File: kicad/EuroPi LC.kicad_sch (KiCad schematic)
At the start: 2 parts, among them U4 MOUDLE-SEEEDUINO-XIAO

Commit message: make 4hp
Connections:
- net VSYS renamed +5V
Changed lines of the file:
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@@
   (junction (at 36.83 55.88) (diameter 0) (color 0 0 0 0)
+  )
+  (wire (pts (xy 114.3 40.64) (xy 114.3 33.02))
+    (stroke (width 0) (type default))
   )
   (wire (pts (xy 121.92 38.1) (xy 121.92 45.72))
@@
   )
   (wire (pts (xy 36.83 55.88) (xy 36.83 63.5))
+    (stroke (width 0) (type default))
+  )
+  (wire (pts (xy 107.95 40.64) (xy 114.3 40.64))
     (stroke (width 0) (type default))
   )
@@
     )
   )
-  (global_label "VSYS" (shape input) (at 107.95 40.64 0) (fields_autoplaced)
-    (effects (font (size 1.27 1.27)) (justify left))
-    (property "Intersheetrefs" "${INTERSHEET_REFS}" (at 115.452 40.64 0)
-      (effects (font (size 1.27 1.27)) (justify left) hide)
-    )
-  )
   (global_label "BUTTON_2" (shape input) (at 67.31 53.34 180) (fields_autoplaced)
     (effects (font (size 1.27 1.27)) (justify right))
@@
         )
       )
+    )
+  )
+  (symbol (lib_id "power:+5V") (at 114.3 33.02 0) (unit 1)
+    (in_bom yes) (on_board yes) (dnp no) (fields_autoplaced)
+    (property "Reference" "#PWR038" (at 114.3 36.83 0)
+      (effects (font (size 1.27 1.27)) hide)
+    )
+    (property "Value" "+5V" (at 114.3 29.21 0)
+      (effects (font (size 1.27 1.27)))
+    )
+    (property "Footprint" "" (at 114.3 33.02 0)
+      (effects (font (size 1.27 1.27)) hide)
+    )
+    (property "Datasheet" "" (at 114.3 33.02 0)
+      (effects (font (size 1.27 1.27)) hide)
+    )
+    (pin "1")
+    (instances
+      (project "EuroPi LC"
+        (path "/1702e620-a749-4340-9e49-cfdb2636cab7/2c8ccfa5-26eb-4a4b-90f9-a487a325ddf4"
+          (reference "#PWR038") (unit 1)
+        )
+        (path "/1702e620-a749-4340-9e49-cfdb2636cab7"
+          (reference "#PWR039") (unit 1)
+        )
+      )

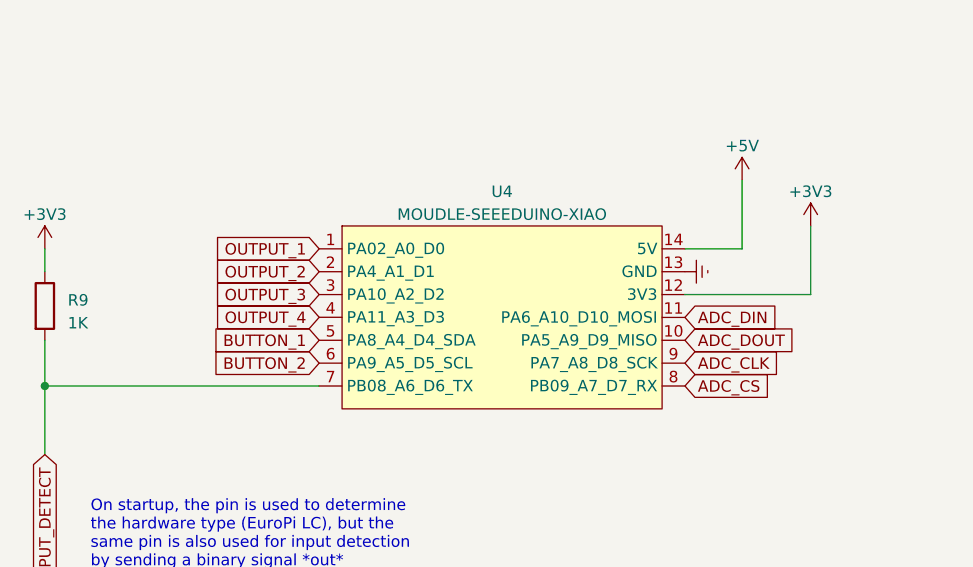
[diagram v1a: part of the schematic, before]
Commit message: input changes
use single channel ADCs for analog inputs and knob 1 which use i2c instead of SPI to free up one pin for input 1 to be used as a digital input as well
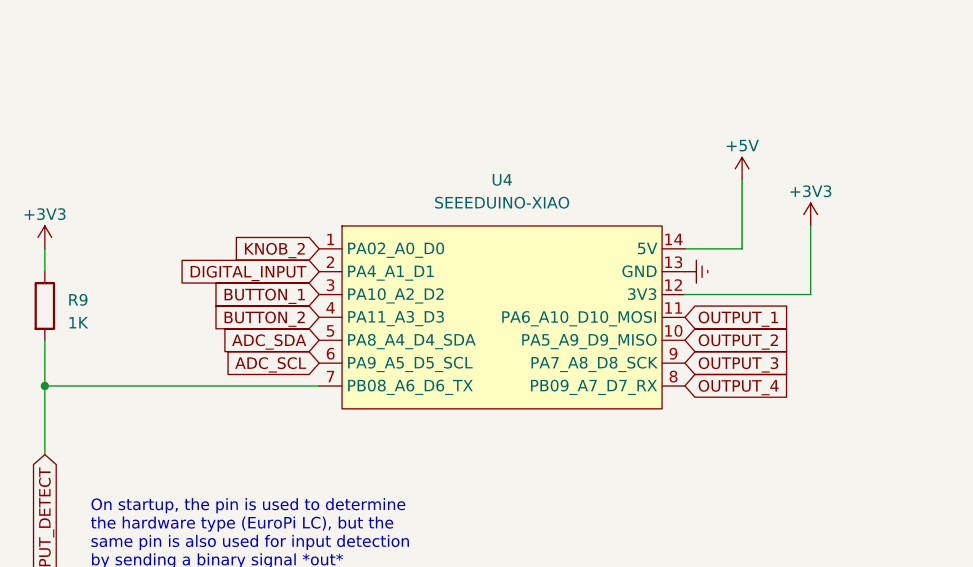
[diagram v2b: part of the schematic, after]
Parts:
- U4: value MOUDLE-SEEEDUINO-XIAO -> SEEEDUINO-XIAO
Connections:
- net ADC_CLK is gone; now on net OUTPUT_3: U4.9 (PA7_A8_D8_SCK)
- net ADC_DIN is gone; now on net OUTPUT_1: U4.11 (PA6_A10_D10_MOSI)
- net ADC_DOUT is gone; now on net OUTPUT_2: U4.10 (PA5_A9_D9_MISO)
- net BUTTON_1: now also U4.3 (PA10_A2_D2); no longer U4.5 (PA8_A4_D4_SDA)
- net BUTTON_2: no longer U4.6 (PA9_A5_D5_SCL)
- net OUTPUT_1: no longer U4.1 (PA02_A0_D0)
- net OUTPUT_2: no longer U4.2 (PA4_A1_D1)
- net OUTPUT_3: no longer U4.3 (PA10_A2_D2)
- net OUTPUT_4: no longer U4.4 (PA11_A3_D3)
- net ADC_CS: no longer names the net of U4.8 (PB09_A7_D7_RX)
- new net ADC_SCL: U4.6 (PA9_A5_D5_SCL)
- new net ADC_SDA: U4.5 (PA8_A4_D4_SDA)
- new net DIGITAL_INPUT: U4.2 (PA4_A1_D1)
- new net KNOB_2: U4.1 (PA02_A0_D0)
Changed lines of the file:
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@@
     (effects (font (size 1.27 1.27)) (justify left bottom))
   )
-  (global_label "ADC_CS" (shape input) (at 107.95 55.88 0) (fields_autoplaced)
-    (effects (font (size 1.27 1.27)) (justify left))
-    (property "Intersheetrefs" "${INTERSHEET_REFS}" (at 117.9315 55.88 0)
-      (effects (font (size 1.27 1.27)) (justify left) hide)
-    )
-  )
-  (global_label "ADC_CLK" (shape input) (at 107.95 53.34 0) (fields_autoplaced)
-    (effects (font (size 1.27 1.27)) (justify left))
-    (property "Intersheetrefs" "${INTERSHEET_REFS}" (at 119.0201 53.34 0)
-      (effects (font (size 1.27 1.27)) (justify left) hide)
-    )
-  )
-  (global_label "OUTPUT_3" (shape input) (at 67.31 45.72 180) (fields_autoplaced)
+  (global_label "OUTPUT_3" (shape input) (at 107.95 53.34 0) (fields_autoplaced)
+    (effects (font (size 1.27 1.27)) (justify left))
+    (property "Intersheetrefs" "${INTERSHEET_REFS}" (at 120.2296 53.34 0)
+      (effects (font (size 1.27 1.27)) (justify left) hide)
+    )
+  )
+  (global_label "OUTPUT_1" (shape input) (at 107.95 48.26 0) (fields_autoplaced)
+    (effects (font (size 1.27 1.27)) (justify left))
+    (property "Intersheetrefs" "${INTERSHEET_REFS}" (at 120.2296 48.26 0)
+      (effects (font (size 1.27 1.27)) (justify left) hide)
+    )
+  )
+  (global_label "INPUT_DETECT" (shape input) (at 36.83 63.5 270) (fields_autoplaced)
+    (effects (font (size 1.27 1.27)) (justify right))
+    (property "Intersheetrefs" "${INTERSHEET_REFS}" (at 36.83 79.65 90)
+      (effects (font (size 1.27 1.27)) (justify right) hide)
+    )
+  )
+  (global_label "OUTPUT_2" (shape input) (at 107.95 50.8 0) (fields_autoplaced)
+    (effects (font (size 1.27 1.27)) (justify left))
+    (property "Intersheetrefs" "${INTERSHEET_REFS}" (at 120.2296 50.8 0)
+      (effects (font (size 1.27 1.27)) (justify left) hide)
+    )
+  )
+  (global_label "KNOB_2" (shape input) (at 67.31 40.64 180) (fields_autoplaced)
+    (effects (font (size 1.27 1.27)) (justify right))
+    (property "Intersheetrefs" "${INTERSHEET_REFS}" (at 57.0261 40.64 0)
+      (effects (font (size 1.27 1.27)) (justify right) hide)
+    )
+  )
+  (global_label "ADC_SCL" (shape input) (at 67.31 53.34 180) (fields_autoplaced)
+    (effects (font (size 1.27 1.27)) (justify right))
+    (property "Intersheetrefs" "${INTERSHEET_REFS}" (at 56.3004 53.34 0)
+      (effects (font (size 1.27 1.27)) (justify right) hide)
+    )
+  )
+  (global_label "BUTTON_1" (shape input) (at 67.31 45.72 180) (fields_autoplaced)
     (effects (font (size 1.27 1.27)) (justify right))
     (property "Intersheetrefs" "${INTERSHEET_REFS}" (at 55.0304 45.72 0)
@@
     )
   )
-  (global_label "OUTPUT_1" (shape input) (at 67.31 40.64 180) (fields_autoplaced)
-    (effects (font (size 1.27 1.27)) (justify right))
-    (property "Intersheetrefs" "${INTERSHEET_REFS}" (at 55.0304 40.64 0)
-      (effects (font (size 1.27 1.27)) (justify right) hide)
-    )
-  )
-  (global_label "INPUT_DETECT" (shape input) (at 36.83 63.5 270) (fields_autoplaced)
-    (effects (font (size 1.27 1.27)) (justify right))
-    (property "Intersheetrefs" "${INTERSHEET_REFS}" (at 36.83 79.65 90)
-      (effects (font (size 1.27 1.27)) (justify right) hide)
-    )
-  )
-  (global_label "OUTPUT_2" (shape input) (at 67.31 43.18 180) (fields_autoplaced)
-    (effects (font (size 1.27 1.27)) (justify right))
-    (property "Intersheetrefs" "${INTERSHEET_REFS}" (at 55.0304 43.18 0)
-      (effects (font (size 1.27 1.27)) (justify right) hide)
-    )
-  )
-  (global_label "BUTTON_1" (shape input) (at 67.31 50.8 180) (fields_autoplaced)
-    (effects (font (size 1.27 1.27)) (justify right))
-    (property "Intersheetrefs" "${INTERSHEET_REFS}" (at 55.0304 50.8 0)
-      (effects (font (size 1.27 1.27)) (justify right) hide)
-    )
-  )
-  (global_label "ADC_DOUT" (shape input) (at 107.95 50.8 0) (fields_autoplaced)
-    (effects (font (size 1.27 1.27)) (justify left))
-    (property "Intersheetrefs" "${INTERSHEET_REFS}" (at 120.3506 50.8 0)
-      (effects (font (size 1.27 1.27)) (justify left) hide)
-    )
-  )
-  (global_label "ADC_DIN" (shape input) (at 107.95 48.26 0) (fields_autoplaced)
-    (effects (font (size 1.27 1.27)) (justify left))
-    (property "Intersheetrefs" "${INTERSHEET_REFS}" (at 118.6573 48.26 0)
-      (effects (font (size 1.27 1.27)) (justify left) hide)
-    )
-  )
-  (global_label "BUTTON_2" (shape input) (at 67.31 53.34 180) (fields_autoplaced)
-    (effects (font (size 1.27 1.27)) (justify right))
-    (property "Intersheetrefs" "${INTERSHEET_REFS}" (at 55.0304 53.34 0)
-      (effects (font (size 1.27 1.27)) (justify right) hide)
-    )
-  )
-  (global_label "OUTPUT_4" (shape input) (at 67.3132 48.2449 180) (fields_autoplaced)
-    (effects (font (size 1.27 1.27)) (justify right))
-    (property "Intersheetrefs" "${INTERSHEET_REFS}" (at 55.0336 48.2449 0)
-      (effects (font (size 1.27 1.27)) (justify right) hide)
+  (global_label "DIGITAL_INPUT" (shape input) (at 67.31 43.18 180) (fields_autoplaced)
+    (effects (font (size 1.27 1.27)) (justify right))
+    (property "Intersheetrefs" "${INTERSHEET_REFS}" (at 51.0993 43.18 0)
+      (effects (font (size 1.27 1.27)) (justify right) hide)
+    )
+  )
+  (global_label "ADC_SDA" (shape input) (at 67.31 50.8 180) (fields_autoplaced)
+    (effects (font (size 1.27 1.27)) (justify right))
+    (property "Intersheetrefs" "${INTERSHEET_REFS}" (at 56.2399 50.8 0)
+      (effects (font (size 1.27 1.27)) (justify right) hide)
+    )
+  )
+  (global_label "BUTTON_2" (shape input) (at 67.31 48.26 180) (fields_autoplaced)
+    (effects (font (size 1.27 1.27)) (justify right))
+    (property "Intersheetrefs" "${INTERSHEET_REFS}" (at 55.0304 48.26 0)
+      (effects (font (size 1.27 1.27)) (justify right) hide)
+    )
+  )
+  (global_label "OUTPUT_4" (shape input) (at 107.9468 55.8649 0) (fields_autoplaced)
+    (effects (font (size 1.27 1.27)) (justify left))
+    (property "Intersheetrefs" "${INTERSHEET_REFS}" (at 120.2264 55.8649 0)
+      (effects (font (size 1.27 1.27)) (justify left) hide)
     )
   )
@@
   (symbol (lib_id "MOUDLE-SEEEDUINO-XIAO:MOUDLE-SEEEDUINO-XIAO") (at 86.36 48.26 0) (unit 1)
     (in_bom yes) (on_board yes) (dnp no) (fields_autoplaced)
-    (property "Reference" "U4" (at 87.63 34.29 0)
-      (effects (font (size 1.27 1.27)))
-    )
-    (property "Value" "MOUDLE-SEEEDUINO-XIAO" (at 87.63 36.83 0)
-      (effects (font (size 1.27 1.27)))
-    )
+    (property "Reference" "U4" (at 87.63 33.02 0)
+      (effects (font (size 1.27 1.27)))
+    )
+    (property "Value" "SEEEDUINO-XIAO" (at 87.63 35.56 0)
+      (effects (font (size 1.27 1.27)))
+    )

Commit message: reroute pcb
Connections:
- net BUTTON_2: now also U4.4 (PA11_A3_D3)
- net OUTPUT_4: now also U4.8 (PB09_A7_D7_RX)
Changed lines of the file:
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@@
     )
   )
-  (global_label "OUTPUT_4" (shape input) (at 107.9468 55.8649 0) (fields_autoplaced)
+  (global_label "OUTPUT_4" (shape input) (at 107.95 55.88 0) (fields_autoplaced)
     (effects (font (size 1.27 1.27)) (justify left))
-    (property "Intersheetrefs" "${INTERSHEET_REFS}" (at 120.2264 55.8649 0)
+    (property "Intersheetrefs" "${INTERSHEET_REFS}" (at 120.2296 55.88 0)
       (effects (font (size 1.27 1.27)) (justify left) hide)
     )

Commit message: add schematic notes
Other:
- note added: "The internal ADC on pin 1 (GP26) is used for knob 2, but knob 1 uses an I2C ADC along with both analogue to free up the spare pin to be used for the digital input"
- note added: "The outputs are simple PWM signals which are smoothed using an RC circuit before being amplified to 0-10V"
- moved on the sheet: R9, U4
